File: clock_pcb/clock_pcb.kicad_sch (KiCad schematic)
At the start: 0 parts

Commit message: finished schematic parts, layout outline
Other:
- removed sheet PAGE2
- removed sheet PAGE3
- added sheet CONNS & PERIPHERALS (PAGE3.kicad_sch)
- added sheet RP2040 & USB (PAGE2.kicad_sch)
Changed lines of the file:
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@@
   (title_block
     (title "Cover Sheet")
-    (date "2022-05-03")
+    (date "2023-06-18")
     (rev "1.0")
   )
-  (text "RP2040 & USB" (at 347.345 29.845 0)
+  (text "RP2040 & USB" (at 255.905 128.27 0)
     (effects (font (size 1.54 1.54) (thickness 0.308) bold) (justify right bottom))
   )
-  (text "FLAT SCHEMATIC SHEETS" (at 304.165 19.685 0)
-    (effects (font (size 2.54 2.54) (thickness 0.508) bold) (justify left bottom))
+  (text "CONNS & PERIPHERALS" (at 256.54 141.605 0)
+    (effects (font (size 1.54 1.54) (thickness 0.308) bold) (justify right bottom))
   )
   (text "RP2040 Clock Base Module" (at 90.17 33.655 0)
     (effects (font (size 5 5) (thickness 0.508) bold) (justify left bottom))
   )
-  (text "CONNS & PERIPHERALS" (at 347.98 43.18 0)
-    (effects (font (size 1.54 1.54) (thickness 0.308) bold) (justify right bottom))
+  (text "FLAT SCHEMATIC SHEETS" (at 212.725 118.11 0)
+    (effects (font (size 2.54 2.54) (thickness 0.508) bold) (justify left bottom))
   )
   (text "#	REV	\n------------------\n1.0	INITIAL RELEASE\n		" (at 213.2076 57.5818 0)
@@
     (effects (font (size 2.54 2.54)) (justify left bottom))
   )
-  (sheet (at 304.8 25.4) (size 44.45 6.35) (fields_autoplaced)
+  (sheet (at 213.36 123.825) (size 44.45 6.35) (fields_autoplaced)
     (stroke (width 0.1524) (type solid))
     (fill (color 0 0 0 0.0000))
-    (property "Sheetname" "PAGE2" (at 304.8 24.6884 0)
+    (property "Sheetname" "RP2040 & USB" (at 213.36 123.1134 0)
       (effects (font (size 1.27 1.27)) (justify left bottom))
     )
-    (property "Sheetfile" "PAGE2.kicad_sch" (at 304.8 32.3346 0)
+    (property "Sheetfile" "PAGE2.kicad_sch" (at 213.36 130.7596 0)
       (effects (font (size 1.27 1.27)) (justify left top))
     )
@@
     )
   )
-  (sheet (at 304.8 38.1) (size 44.45 6.35) (fields_autoplaced)
+  (sheet (at 213.36 136.525) (size 44.45 6.35) (fields_autoplaced)
     (stroke (width 0.1524) (type solid))
     (fill (color 0 0 0 0.0000))
-    (property "Sheetname" "PAGE3" (at 304.8 37.3884 0)
+    (property "Sheetname" "CONNS & PERIPHERALS" (at 213.36 135.8134 0)
       (effects (font (size 1.27 1.27)) (justify left bottom))
     )
-    (property "Sheetfile" "PAGE3.kicad_sch" (at 304.8 45.0346 0)
+    (property "Sheetfile" "PAGE3.kicad_sch" (at 213.36 143.4596 0)
       (effects (font (size 1.27 1.27)) (justify left top))
     )

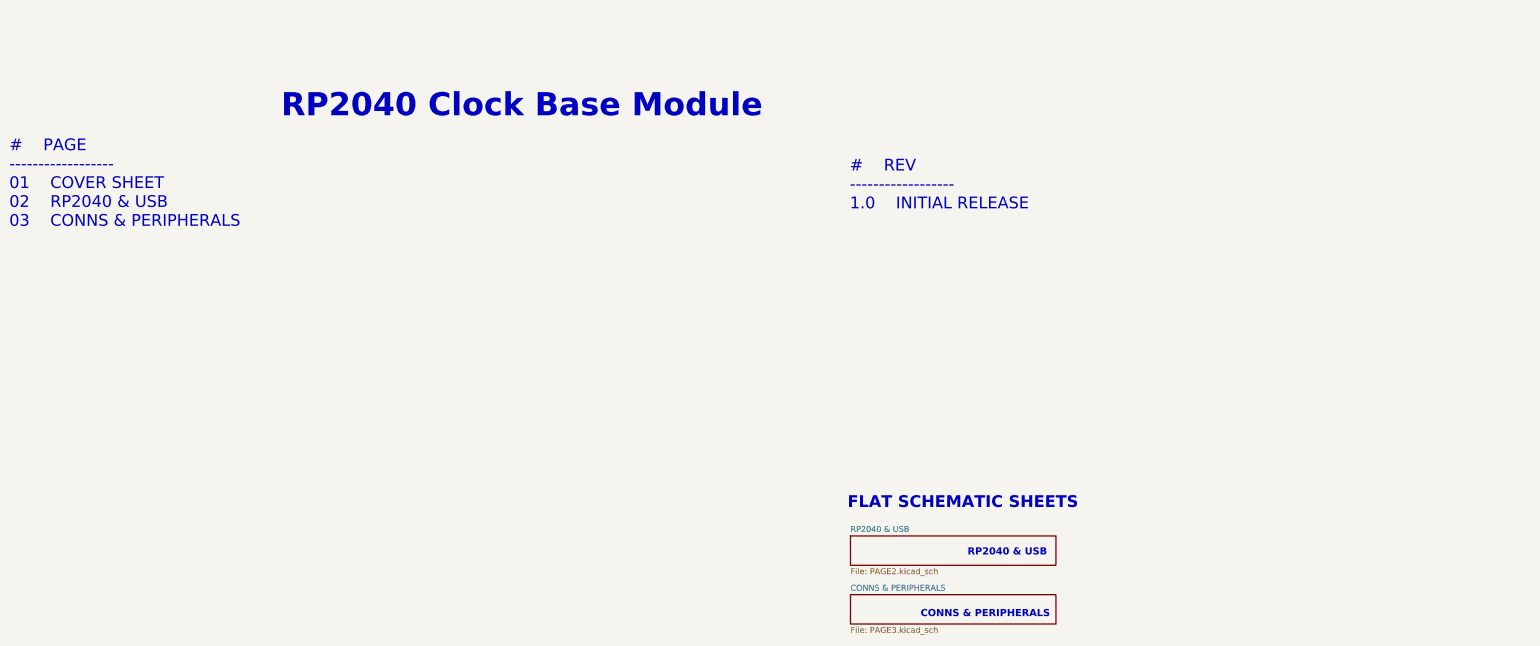
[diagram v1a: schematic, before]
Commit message: fusion360 assm is not nice
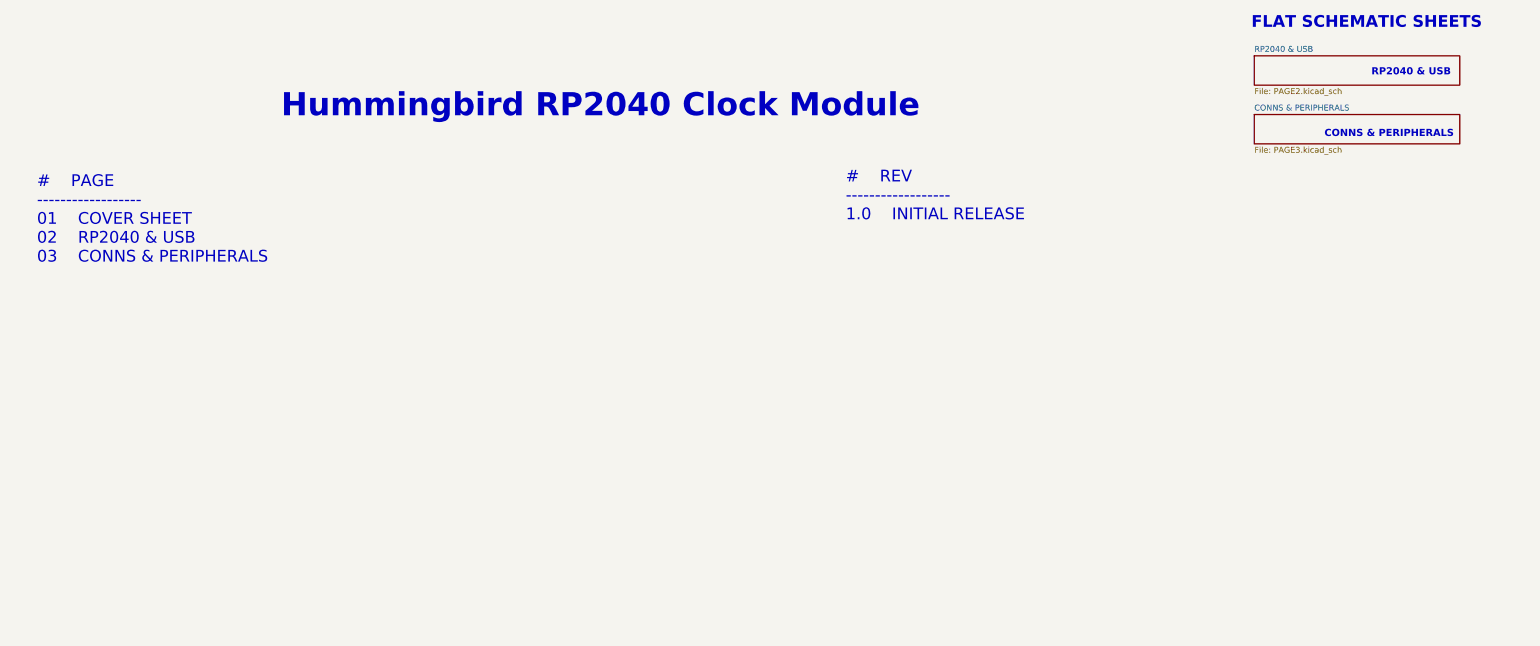
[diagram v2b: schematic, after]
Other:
- note added: "Hummingbird RP2040 Clock Module"
- note removed: "RP2040 Clock Base Module"
